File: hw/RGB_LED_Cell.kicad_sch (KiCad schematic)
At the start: 4 parts

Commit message: annotations
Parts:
- gave numbers to parts that had none: 4

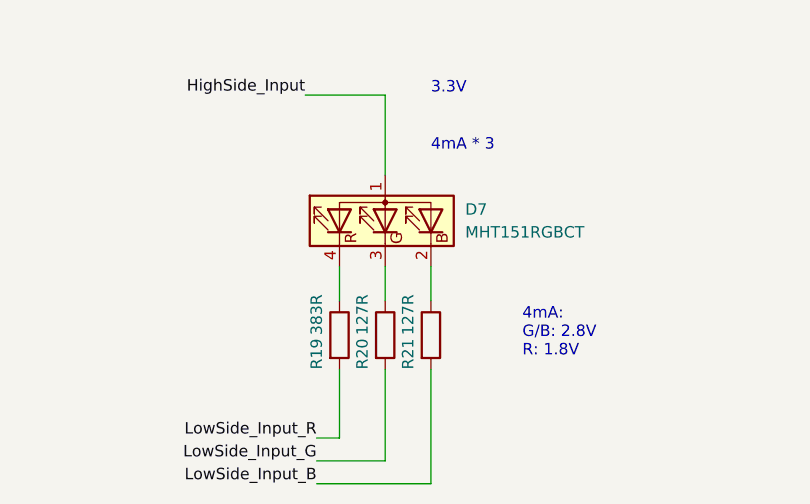
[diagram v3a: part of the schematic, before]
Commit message: updated RGB_LED_CELL due to paths
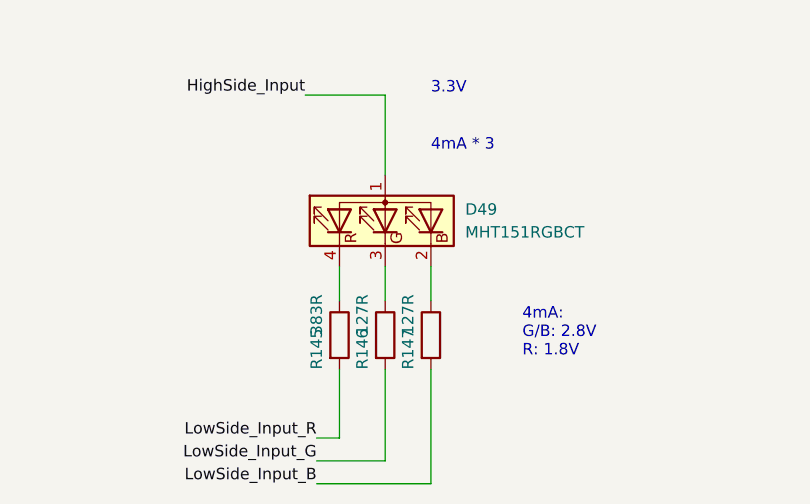
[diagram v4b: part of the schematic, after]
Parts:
- renumbered D7 to D49, R19 to R145, R20 to R146, R21 to R147

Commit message: fix issues in schematic and footprints
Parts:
- D49: footprint LED_SMD:LED_1206_3216Metric_ReverseMount_Hole1.8x2.4mm -> IotPi_LED:MeiHua_RGB_LED_Reverse_Mounting_MHT151RGBCT
